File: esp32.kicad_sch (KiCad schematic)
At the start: 13 parts, among them SW1 RESET, SW2 CASE, SW3 BOOT, U3 ESP32-S3-WROOM-1

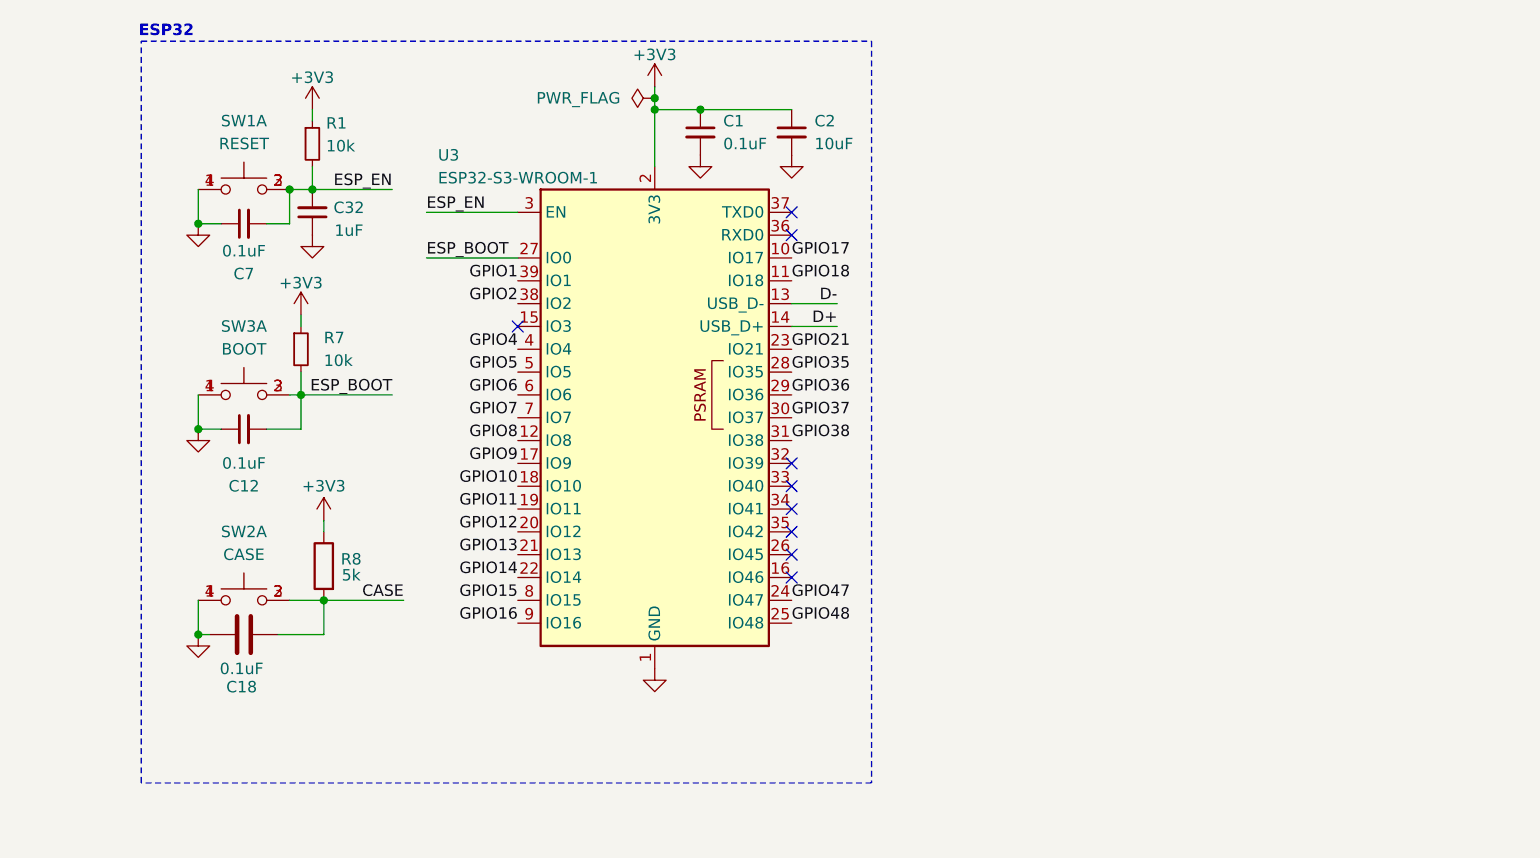
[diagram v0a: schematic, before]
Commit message: added global labels
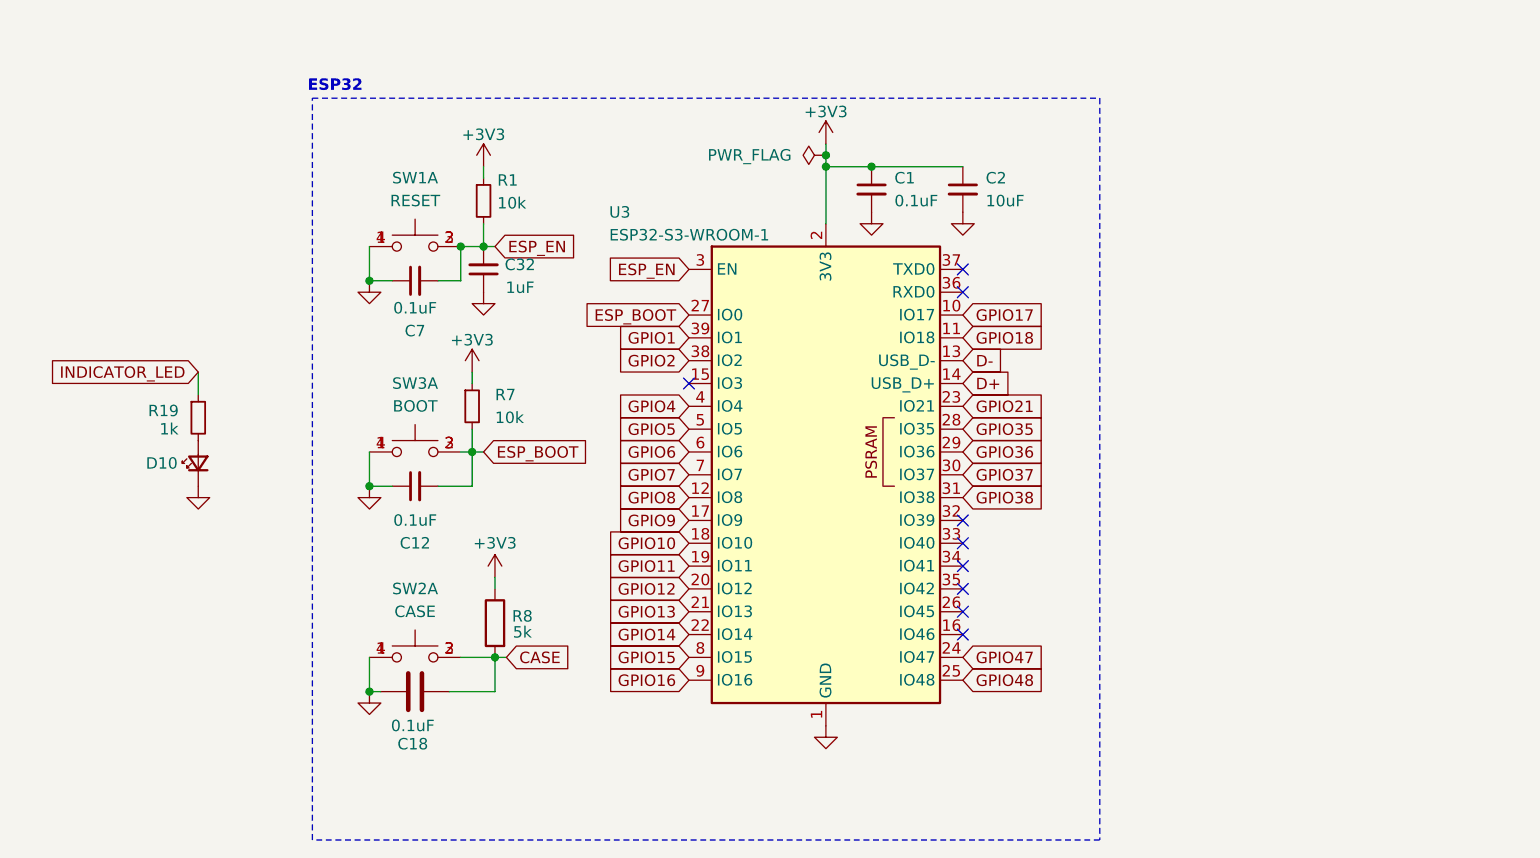
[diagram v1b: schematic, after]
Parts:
- added D10: LED_Small, LED_SMD:LED_0603_1608Metric, symbol Device:LED_Small
- added R19: 1k, Resistor_SMD:R_0603_1608Metric, symbol Device:R_Small
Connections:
- net GND: now also D10.1 (K)
- new net: D10.2 (A), R19.2
- new net INDICATOR_LED: R19.1
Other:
- moved on the sheet: C1, C12, C18, C2, C32, C7, R1, R7, R8, SW1A, SW2A, SW3A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

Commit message: added PDFs
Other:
- title: (none) -> Minisumo PCB
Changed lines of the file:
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@@
 	(generator_version "9.0")
 	(paper "A4")
+	(title_block
+		(title "Minisumo PCB")
+		(date "2025-04-16")
+		(rev "3.2")
+		(comment 2 "alex_ivan1304@outlook.com")
+		(comment 3 "Designed by: Ivan Alexandru Marian")
+	)
 	(rectangle
 		(start 99.06 52.07)

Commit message: custom
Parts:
- R19: value 1k -> 10k
- R8: value 5k -> 10k
- SW1, SW2, SW3: M_NUMBER 710-435441019830 -> 688-SKRPACE010
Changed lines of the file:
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@@
 	(rectangle
 		(start 99.06 52.07)
-		(end 186.69 134.62)
+		(end 233.68 134.62)
 		(stroke
 			(width 0)
@@
 			)
 		)
-		(property "Value" "5k"
+		(property "Value" "10k"
 			(at 122.428 111.506 0)
 			(effects
@@
 			)
 		)
-		(property "M_NUMBER" "710-435441019830"
+		(property "M_NUMBER" "688-SKRPACE010"
 			(at 110.49 91.44 0)
 			(effects
@@
 			)
 		)
-		(property "M_NUMBER" "710-435441019830"
+		(property "M_NUMBER" "688-SKRPACE010"
 			(at 110.49 68.58 0)
 			(effects
@@
 			)
 		)
-		(property "M_NUMBER" "710-435441019830"
+		(property "M_NUMBER" "688-SKRPACE010"
 			(at 110.49 114.3 0)
 			(effects
@@
 			)
 		)
-		(property "Value" "1k"
+		(property "Value" "10k"
 			(at 82.042 88.9 0)
 			(effects
